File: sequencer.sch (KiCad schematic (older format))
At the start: 0 parts

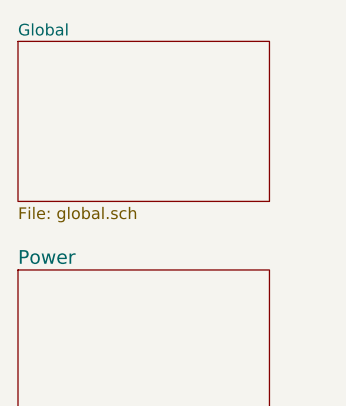
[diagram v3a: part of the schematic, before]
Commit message: revised schematic and pcb
- fixed clock/reset inputs
- schematic annotations
- moved to cc-by-nc-sa
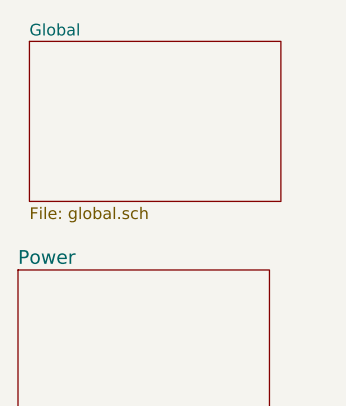
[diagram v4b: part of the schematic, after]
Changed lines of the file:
@@
 $EndDescr
 $Sheet
-S 700  700  1100 700
+S 750  700  1100 700
 U 5AF89FF5
 F0 "Global" 51
